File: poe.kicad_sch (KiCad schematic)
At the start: 57 parts, among them Q1 Si7430DP, U1 MP8008, U10 MagJack-A70-112-331N126, U2 LTV-817S, U3 750310744, U6 TL432DBZ, U7 TPD4EUSB30, U8 TPD4EUSB30

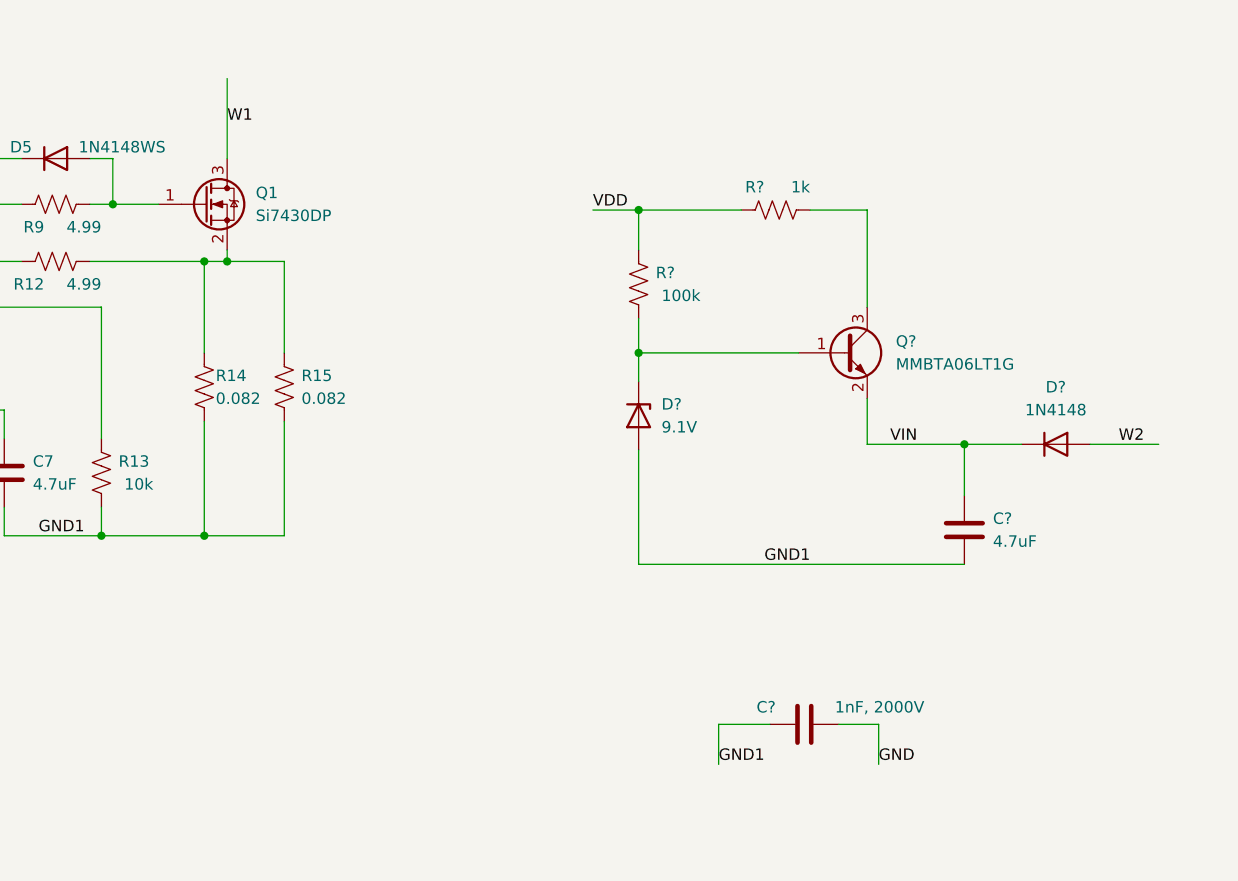
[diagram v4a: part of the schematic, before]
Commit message: added flyback mosfet footprint
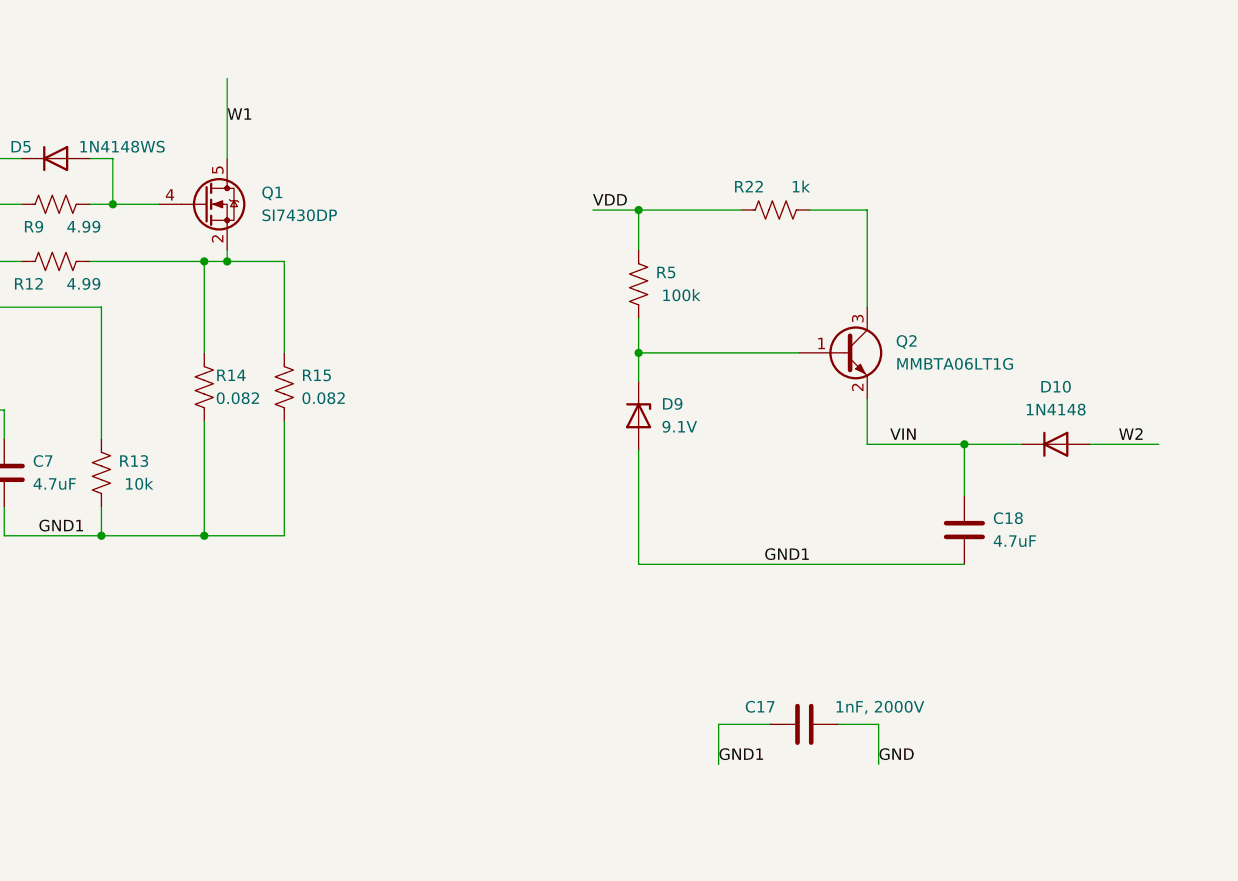
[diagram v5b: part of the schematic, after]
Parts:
- removed Q1: Si7430DP, symbol Transistor_FET:DMN67D8L
- added Q1: SI7430DP, bitcart:SI7430DP, symbol bitcart:SI7430DP
- gave numbers to parts that had none: 7
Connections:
- net W1: now also Q1.5 (D)
- net at D5.2 (A), R9.1: now also Q1.4 (G)
- net at R12.1, R14.2, R15.2: now also Q1.1 (S), Q1.2 (S), Q1.3 (S)
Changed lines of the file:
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@@
   (symbol (lib_id "Device:R_US") (at 205.74 56.515 270) (unit 1)
     (in_bom yes) (on_board yes)
-    (property "Reference" "R?" (id 0) (at 204.47 53.975 90)
+    (property "Reference" "R22" (id 0) (at 204.47 53.975 90)
       (effects (font (size 1.27 1.27)) (justify right))
     )
@@
     (pin "4")
   )
-  (symbol (lib_id "Transistor_FET:DMN67D8L") (at 142.24 55.88 0) (unit 1)
-    (in_bom yes) (on_board yes)
-    (property "Reference" "Q1" (id 0) (at 147.955 54.61 0)
-      (effects (font (size 1.27 1.27)) (justify left))
-    )
-    (property "Value" "Si7430DP" (id 1) (at 147.955 57.15 0)
-      (effects (font (size 1.27 1.27)) (justify left))
-    )
-    (property "Footprint" "" (id 2) (at 147.32 57.785 0)
-      (effects (font (size 1.27 1.27) italic) (justify left) hide)
-    )
-    (property "Datasheet" "https://www.mouser.com/datasheet/2/427/VISH_S_A0001702753_1-2567400.pdf" (id 3) (at 142.24 55.88 0)
-      (effects (font (size 1.27 1.27)) (justify left) hide)
-    )
-    (property "PARTNO" "SI7430DP-T1-GE3" (id 4) (at 142.24 55.88 0)
-      (effects (font (size 1.27 1.27)) hide)
-    )
-    (property "ME" "781-SI7430DP-T1-GE3" (id 5) (at 142.24 55.88 0)
-      (effects (font (size 1.27 1.27)) hide)
-    )
-    (pin "1")
-    (pin "2")
-    (pin "3")
-  )
   (symbol (lib_id "Device:D_Bridge_+-AA") (at 340.995 121.285 90) (unit 1)
     (in_bom yes) (on_board yes)
@@
   (symbol (lib_id "Device:R_US") (at 190.5 64.77 180) (unit 1)
     (in_bom yes) (on_board yes)
-    (property "Reference" "R?" (id 0) (at 192.405 63.5 0)
+    (property "Reference" "R5" (id 0) (at 192.405 63.5 0)
       (effects (font (size 1.27 1.27)) (justify right))
     )
@@
     (pin "1")
     (pin "2")
+  )
+  (symbol (lib_id "bitcart:SI7430DP") (at 142.24 55.88 0) (unit 1)
+    (in_bom yes) (on_board yes) (fields_autoplaced)
+    (property "Reference" "Q1" (id 0) (at 148.59 54.6099 0)
+      (effects (font (size 1.27 1.27)) (justify left))
+    )
+    (property "Value" "SI7430DP" (id 1) (at 148.59 57.1499 0)
+      (effects (font (size 1.27 1.27)) (justify left))
+    )
+    (property "Footprint" "bitcart:SI7430DP" (id 2) (at 147.32 41.91 0)
+      (effects (font (size 1.27 1.27) italic) (justify left) hide)
+    )
+    (property "Datasheet" "https://www.mouser.com/datasheet/2/427/VISH_S_A0001702753_1-2567400.pdf" (id 3) (at 147.32 39.37 0)
+      (effects (font (size 1.27 1.27)) (justify left) hide)
+    )
+    (property "PARTNO" "SI7430DP-T1-GE3" (id 4) (at 142.24 55.88 0)
+      (effects (font (size 1.27 1.27)) hide)
+    )
+    (property "ME" "781-SI7430DP-T1-GE3" (id 5) (at 142.24 55.88 0)
+      (effects (font (size 1.27 1.27)) hide)
+    )
+    (pin "1")
+    (pin "2")
+    (pin "3")
+    (pin "4")
+    (pin "5")
   )
   (symbol (lib_id "Device:D") (at 118.11 162.56 0) (unit 1)
@@
   (symbol (lib_id "Device:C") (at 208.915 113.665 90) (unit 1)
     (in_bom yes) (on_board yes)
-    (property "Reference" "C?" (id 0) (at 205.74 111.76 90)
+    (property "Reference" "C17" (id 0) (at 205.74 111.76 90)
       (effects (font (size 1.27 1.27)) (justify left))
     )
@@
   (symbol (lib_id "Device:D_Zener") (at 190.5 79.375 270) (unit 1)
     (in_bom yes) (on_board yes) (fields_autoplaced)
-    (property "Reference" "D?" (id 0) (at 193.04 78.1049 90)
+    (property "Reference" "D9" (id 0) (at 193.04 78.1049 90)
       (effects (font (size 1.27 1.27)) (justify left))
     )
@@
   (symbol (lib_id "Diode:1N4148") (at 236.855 82.55 0) (unit 1)
     (in_bom yes) (on_board yes) (fields_autoplaced)
-    (property "Reference" "D?" (id 0) (at 236.855 76.2 0))
+    (property "Reference" "D10" (id 0) (at 236.855 76.2 0))
     (property "Value" "1N4148" (id 1) (at 236.855 78.74 0))
     (property "Footprint" "Diode_THT:D_DO-35_SOD27_P7.62mm_Horizontal" (id 2) (at 236.855 86.995 0)
@@
   (symbol (lib_id "Transistor_BJT:MMBTA42") (at 213.36 72.39 0) (unit 1)
     (in_bom yes) (on_board yes) (fields_autoplaced)
-    (property "Reference" "Q?" (id 0) (at 219.075 71.1199 0)
+    (property "Reference" "Q2" (id 0) (at 219.075 71.1199 0)
       (effects (font (size 1.27 1.27)) (justify left))
     )
@@
   (symbol (lib_id "Device:C") (at 226.695 92.075 0) (unit 1)
     (in_bom yes) (on_board yes)
-    (property "Reference" "C?" (id 0) (at 229.87 90.805 0)
-      (effects (font (size 1.27 1.27)) (justify left))
-    )
+    (property "Reference" "C18" (id 0) (at 229.87 90.805 0)
+      (effects (font (size 1.27 1.27)) (justify left))
+    )

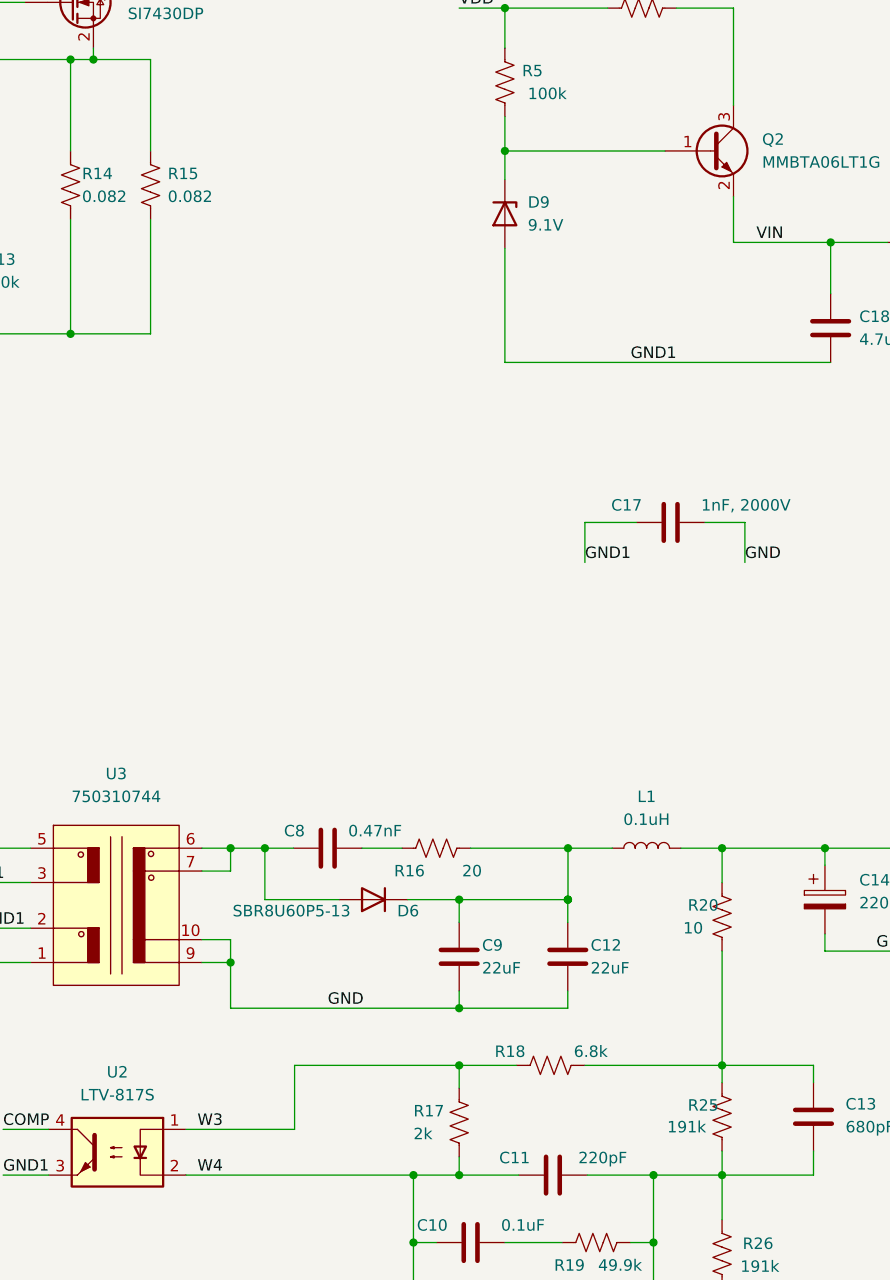
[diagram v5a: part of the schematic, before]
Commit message: added a bunch more PoE footprints
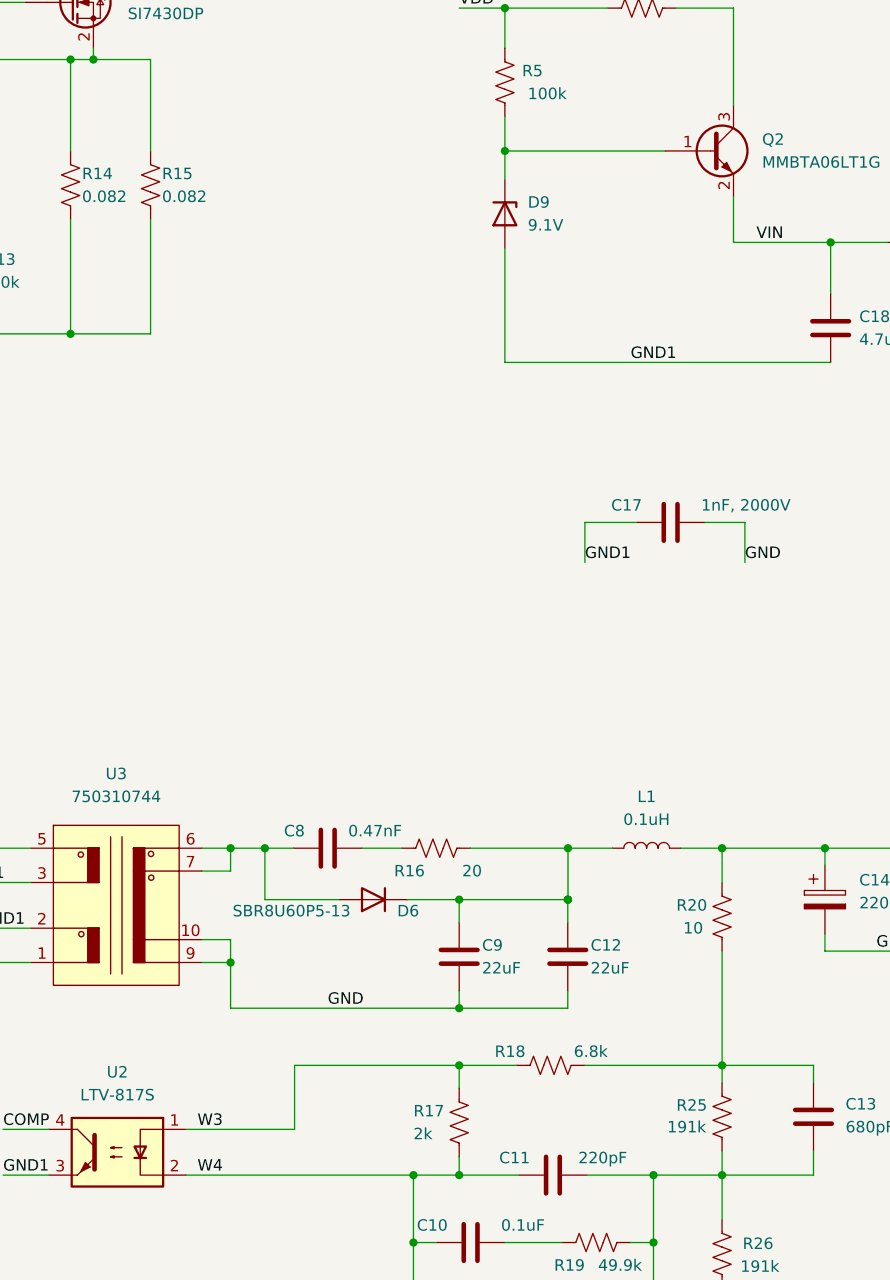
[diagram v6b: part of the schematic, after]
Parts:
- C1: footprint (none) -> Resistor_SMD:R_1206_3216Metric; DK (none) -> 490-3364-1-ND; PARTNO (none) -> GRM319R72A104KA01D
- C6: footprint (none) -> Capacitor_SMD:C_0603_1608Metric; PARTNO (none) -> GRM188R71H224KA93D
- C7: footprint (none) -> Capacitor_SMD:C_0805_2012Metric; PARTNO (none) -> GRM21BR71C475KA73L
- D3: footprint (none) -> Diode_SMD:D_SMA; DK (none) -> SMAJ58ALFCT-ND; PARTNO (none) -> SMAJ58A
- D5: footprint (none) -> Diode_SMD:D_SOD-323; PARTNO (none) -> 1N4148WS-7
- R12, R13, R17, R18, R19, R2, R20, R22, R25, R26, R3, R4, R5, R9: footprint (none) -> Resistor_SMD:R_0603_1608Metric
- R14, R15: footprint (none) -> Resistor_SMD:R_1206_3216Metric; DK (none) -> 273-KDV12FR082ETCT-ND; PARTNO (none) -> KDV12FR082ET
- R16: footprint (none) -> Resistor_SMD:R_0805_2012Metric; DK (none) -> 311-20ARCT-ND; PARTNO (none) -> RC0805JR-0720RL
- R6, R7: footprint (none) -> Resistor_SMD:R_1206_3216Metric; DK (none) -> 311-20KERCT-ND; PARTNO (none) -> RC1206JR-0720KL

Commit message: yet more PoE footprints
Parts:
- removed D10: 1N4148, Diode_THT:D_DO-35_SOD27_P7.62mm_Horizontal, symbol Diode:1N4148
- added D11: 1N4148WS, Diode_SMD:D_SOD-323, symbol Device:D
- C10, C15: footprint (none) -> Capacitor_SMD:C_0603_1608Metric; DK (none) -> 478-10346-1-ND; PARTNO (none) -> 06035C104KAT4A
- C11: footprint (none) -> Capacitor_SMD:C_0603_1608Metric; PARTNO (none) -> GRM188R71H221KA01D
- C12, C9: footprint (none) -> Capacitor_SMD:C_1210_3225Metric; DK (none) -> 490-5313-1-ND; PARTNO (none) -> GRM32ER71E226KE15L
- C13: footprint (none) -> Capacitor_SMD:C_0603_1608Metric; PARTNO (none) -> GRM188R71H681KA01D
- C14: footprint (none) -> Capacitor_SMD:CP_Elec_8x10.5; DK (none) -> 732-8441-1-ND; PARTNO (none) -> 865080453013
- C17: footprint (none) -> Capacitor_SMD:C_1812_4532Metric; DK (none) -> 490-8145-1-ND; PARTNO (none) -> GR442QR73D102KW01L
- C18: value 4.7uF -> 1uF; footprint (none) -> Capacitor_SMD:C_0603_1608Metric; PARTNO (none) -> GRM188R71E105KA61D
- C2: footprint (none) -> Capacitor_SMD:CP_Elec_10x10.5; DK (none) -> 1572-1483-1-ND; PARTNO (none) -> 476SML100M
- C8: footprint (none) -> Capacitor_SMD:C_0603_1608Metric; PARTNO (none) -> GRM188R72A471KA01D
- D4: footprint (none) -> Diode_SMD:D_SOD-123F; DK (none) -> BAV21WRHGCT-ND; PARTNO (none) -> BAV21W RHG
- D6: footprint (none) -> bitcart:SBR8U60P5-13; DK (none) -> SBR8U60P5DICT-ND; PARTNO (none) -> SBR8U60P5-13
- D9: footprint (none) -> Diode_SMD:D_SOD-123; DK (none) -> 3757-BZT52-C9V1_R1_00001CT-ND; PARTNO (none) -> BZT52-C9V1_R1_00001
- Q2: DK (none) -> MMBTA06LT1GOSCT-ND; PARTNO (none) -> MMBTA06LT1G
- U2: value LTV-817S -> FOD817S; DK (none) -> FOD817SDCT-ND; PARTNO (none) -> FOD817SD
- U6: DK (none) -> TL432ASA-7DICT-ND; PARTNO (none) -> TL432ASA-7
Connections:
- net VIN: now also D11.1 (K)
- net W2: now also D11.2 (A)

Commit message: all footprints added?!
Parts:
- removed D6: SBR8U60P5-13, bitcart:SBR8U60P5-13, symbol Device:D
- added D6: SBR8U60P5-13, bitcart:SBR8U60P5-13, symbol bitcart:SBR8U60P5-13
- C3, C4: footprint (none) -> Capacitor_SMD:C_1210_3225Metric; DK (none) -> 490-3385-1-ND; PARTNO (none) -> GRM32ER72A225KA35L
- C5: value 100nF -> 0.1uF; footprint (none) -> Capacitor_SMD:C_0805_2012Metric; DK (none) -> 490-12005-1-ND; PARTNO (none) -> GRM21BR72A104KAC4L
- U3: ME (none) -> 710-750310744
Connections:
- net GND1: now also U1.29 (EP)
- net at C8.1, U3.6, U3.7: now also D6.2 (A), D6.3 (A)
- net at C12.1, C9.1, L1.1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: now also D6.1 (K)
